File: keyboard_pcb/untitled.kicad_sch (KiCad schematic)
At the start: 39 parts, among them J1 USB_C_Receptacle_USB2.0_16P, J2 Conn_01x02, J3 SWD, SW1 Reset, U1 NCP1117-3.3_SOT223, U2 RP2040, U3 W25Q128JVS, Y1 Crystal_GND24

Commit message: completed all routing and ground fill
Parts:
- H1, H2, H3, H4: footprint Components:L60 Outline -> MountingHole:MountingHole_2.2mm_M2_DIN965_Pad
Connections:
- net RESET is gone; now on net Run: J3.1 (Pin_1)
- net SWDIO is gone; now on net SWD: J3.4 (Pin_4)
- net Run: now also U2.26 (RUN)
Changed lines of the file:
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@@
 	(wire
 		(pts
+			(xy 133.35 95.25) (xy 146.05 95.25)
+		)
+		(stroke
+			(width 0)
+			(type default)
+		)
+	)
+	(wire
+		(pts
 			(xy 41.91 22.86) (xy 64.77 22.86)
 		)
@@
 	(wire
 		(pts
+			(xy 133.35 92.71) (xy 146.05 92.71)
+		)
+		(stroke
+			(width 0)
+			(type default)
+		)
+	)
+	(wire
+		(pts
 			(xy 252.73 53.34) (xy 262.89 53.34)
 		)
@@
 	(wire
 		(pts
+			(xy 139.7 85.09) (xy 146.05 85.09)
+		)
+		(stroke
+			(width 0)
+			(type default)
+		)
+	)
+	(wire
+		(pts
 			(xy 97.79 44.45) (xy 97.79 46.99)
 		)
@@
 	(wire
 		(pts
+			(xy 195.58 53.34) (xy 201.93 53.34)
+		)
+		(stroke
+			(width 0)
+			(type default)
+		)
+	)
+	(wire
+		(pts
 			(xy 44.45 148.59) (xy 50.8 148.59)
 		)
@@
 	(wire
 		(pts
-			(xy 134.62 90.17) (xy 146.05 90.17)
+			(xy 125.73 90.17) (xy 146.05 90.17)
 		)
 		(stroke
@@
 		)
 	)
+	(label "Run"
+		(at 195.58 53.34 0)
+		(effects
+			(font
+				(size 1.27 1.27)
+			)
+			(justify left bottom)
+		)
+	)
 	(label "QSPI_SCLK"
 		(at 191.77 86.36 0)
@@
 		)
 	)
+	(label "Run"
+		(at 139.7 85.09 0)
+		(effects
+			(font
+				(size 1.27 1.27)
+			)
+			(justify left bottom)
+		)
+	)
 	(label "QSPI_SD1"
 		(at 191.77 78.74 0)
@@
 		)
 	)
+	(label "SWD"
+		(at 133.35 92.71 0)
+		(effects
+			(font
+				(size 1.27 1.27)
+			)
+			(justify left bottom)
+		)
+	)
 	(label "XOUT"
 		(at 64.77 40.64 180)
@@
 		)
 	)
+	(label "SWCLK"
+		(at 133.35 95.25 0)
+		(effects
+			(font
+				(size 1.27 1.27)
+			)
+			(justify left bottom)
+		)
+	)
 	(label "XIN"
 		(at 64.77 22.86 180)
@@
 		)
 	)
-	(global_label "SWDIO"
-		(shape input)
-		(at 146.05 92.71 180)
-		(fields_autoplaced yes)
-		(effects
-			(font
-				(size 1.27 1.27)
-			)
-			(justify right)
-		)
-		(property "Intersheetrefs" "${INTERSHEET_REFS}"
-			(at 137.7707 92.6306 0)
-			(effects
-				(font
-					(size 1.27 1.27)
-				)
-				(justify right)
-				(hide yes)
-			)
-		)
-	)
 	(global_label "col1"
 		(shape input)
@@
 		)
 	)
-	(global_label "SWCLK"
-		(shape input)
-		(at 146.05 95.25 180)
-		(fields_autoplaced yes)
-		(effects
-			(font
-				(size 1.27 1.27)
-			)
-			(justify right)
-		)
-		(property "Intersheetrefs" "${INTERSHEET_REFS}"
-			(at 137.4079 95.1706 0)
-			(effects
-				(font
-					(size 1.27 1.27)
-				)
-				(justify right)
-				(hide yes)
-			)
-		)
-	)
-	(global_label "RESET"
-		(shape input)
-		(at 146.05 85.09 180)
-		(fields_autoplaced yes)
-		(effects
-			(font
-				(size 1.27 1.27)
-			)
-			(justify right)
-		)
-		(property "Intersheetrefs" "${INTERSHEET_REFS}"
-			(at 137.8917 85.0106 0)
-			(effects
-				(font
-					(size 1.27 1.27)
-				)
-				(justify right)
-				(hide yes)
-			)
-		)
-	)
 	(global_label "LED"
 		(shape input)
@@
 			)
 		)
-		(property "Footprint" "Components:L60 Outline"
+		(property "Footprint" "MountingHole:MountingHole_2.2mm_M2_DIN965_Pad"
 			(at 135.89 128.27 0)
 			(effects
@@
 			)
 		)
-		(property "Footprint" "Components:L60 Outline"
+		(property "Footprint" "MountingHole:MountingHole_2.2mm_M2_DIN965_Pad"
 			(at 116.84 128.27 0)
 			(effects
@@
 	(symbol
 		(lib_id "power:GND")
-		(at 134.62 90.17 0)
+		(at 125.73 90.17 0)
 		(unit 1)
 		(exclude_from_sim no)
@@
 		(dnp no)
 		(property "Reference" "#PWR040"
-			(at 134.62 96.52 0)
+			(at 125.73 96.52 0)
 			(effects
 				(font
@@
 		)
 		(property "Value" "GND"
-			(at 134.62 93.98 0)
+			(at 125.73 93.98 0)
 			(effects
 				(font
@@
 		)
 		(property "Footprint" ""
-			(at 134.62 90.17 0)
+			(at 125.73 90.17 0)
 			(effects
 				(font
@@
 		)
 		(property "Datasheet" ""
-			(at 134.62 90.17 0)
+			(at 125.73 90.17 0)
 			(effects
 				(font
@@
 		)
 		(property "Description" ""
-			(at 134.62 90.17 0)
+			(at 125.73 90.17 0)
 			(effects
 				(font
@@
 			)
 		)
-		(property "Footprint" "Components:L60 Outline"
+		(property "Footprint" "MountingHole:MountingHole_2.2mm_M2_DIN965_Pad"
 			(at 135.89 116.84 0)
 			(effects
@@
 			)
 		)
-		(property "Footprint" "Components:L60 Outline"
+		(property "Footprint" "MountingHole:MountingHole_2.2mm_M2_DIN965_Pad"
 			(at 116.84 116.84 0)
 			(effects

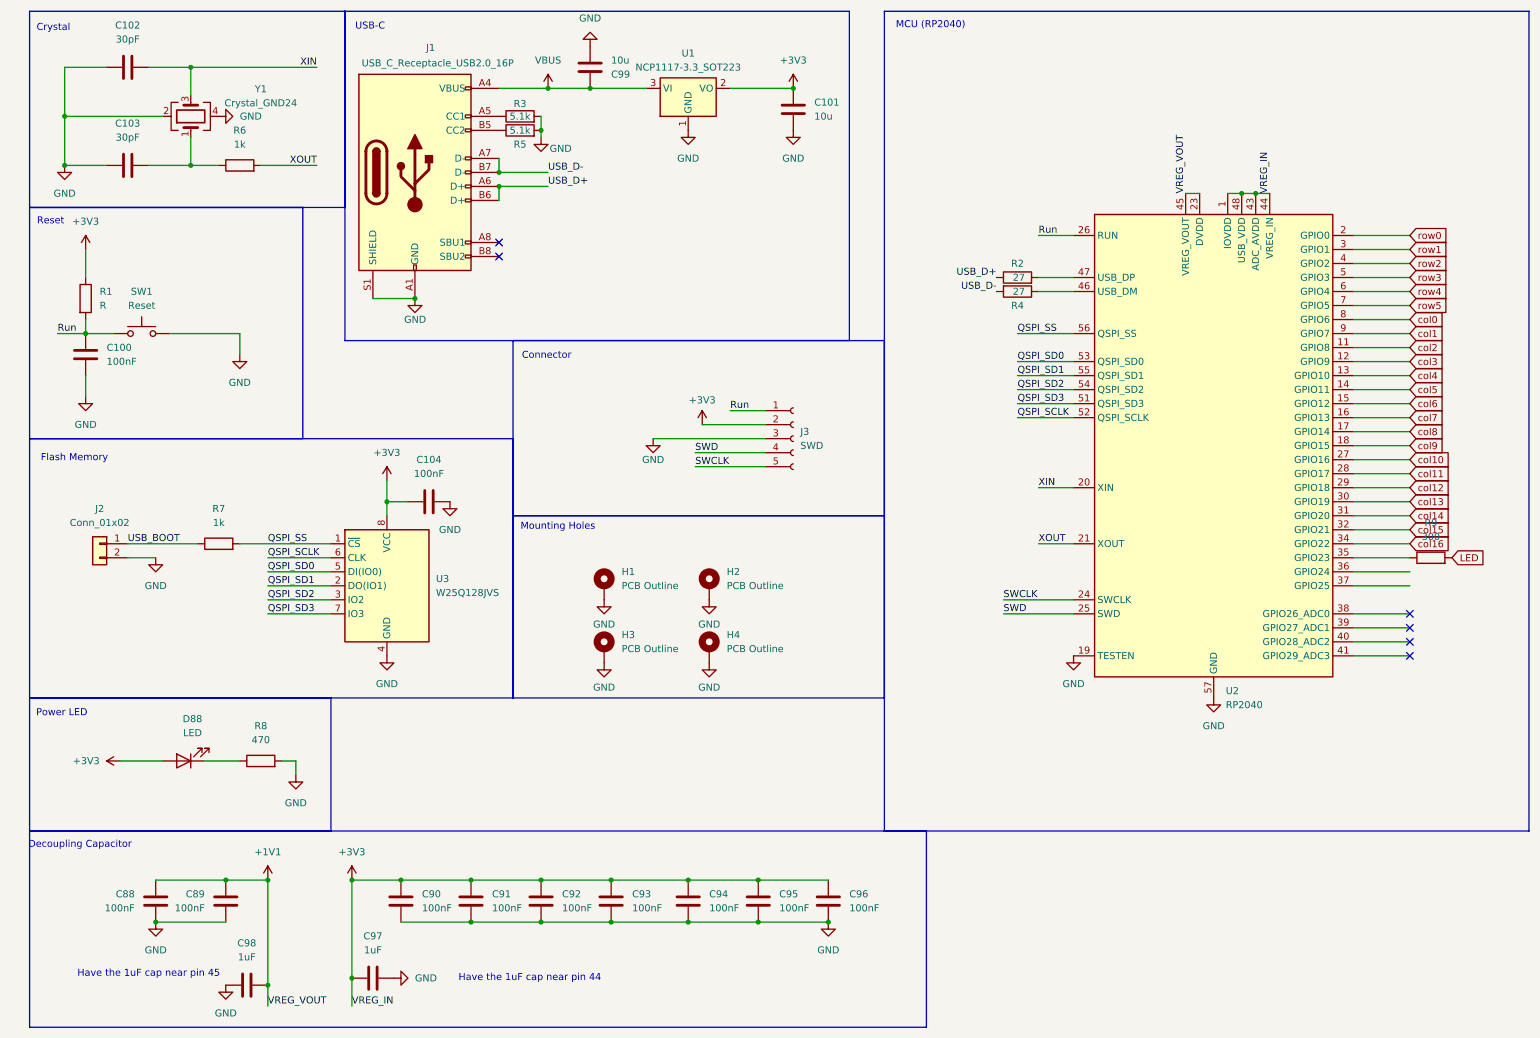
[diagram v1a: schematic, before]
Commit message: edited power supply circuits
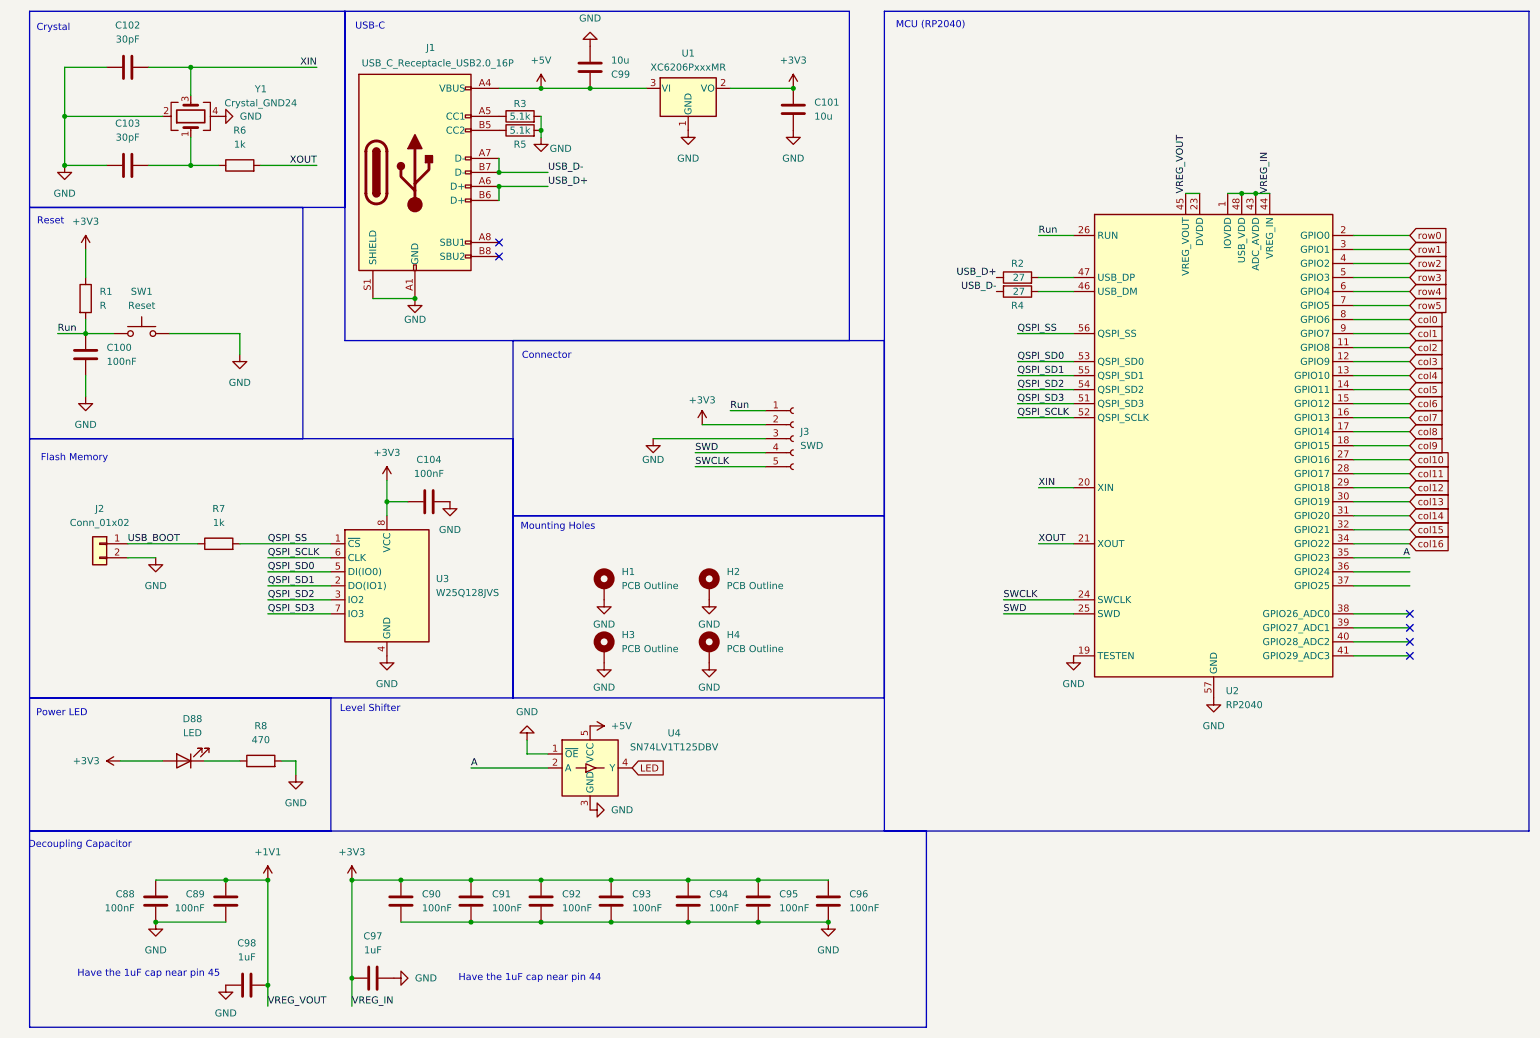
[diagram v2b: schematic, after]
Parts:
- removed R9: 300, Resistor_SMD:R_0603_1608Metric_Pad0.98x0.95mm_HandSolder, symbol Device:R
- removed U1: NCP1117-3.3_SOT223, Package_TO_SOT_SMD:SOT-223-3_TabPin2, symbol Regulator_Linear:NCP1117-3.3_SOT223
- added U1: XC6206PxxxMR, Package_TO_SOT_SMD:SOT-23-3, symbol Regulator_Linear:XC6206PxxxMR
- added U4: SN74LV1T125DBV, Package_TO_SOT_SMD:SOT-23-5, symbol Logic_LevelTranslator:SN74LV1T125DBV
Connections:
- net +3V3: now also U1.2 (VO)
- net GND: now also U1.1 (GND), U4.1 (~{OE}), U4.3 (GND)
- net LED: now also U4.4 (Y)
- net A: now reaches U2.35 (GPIO23)
- net A: now also U4.2 (A)
- net VBUS renamed +5V
- net +5V: now also U1.3 (VI), U4.5 (VCC)
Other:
- note added: "Level Shifter"

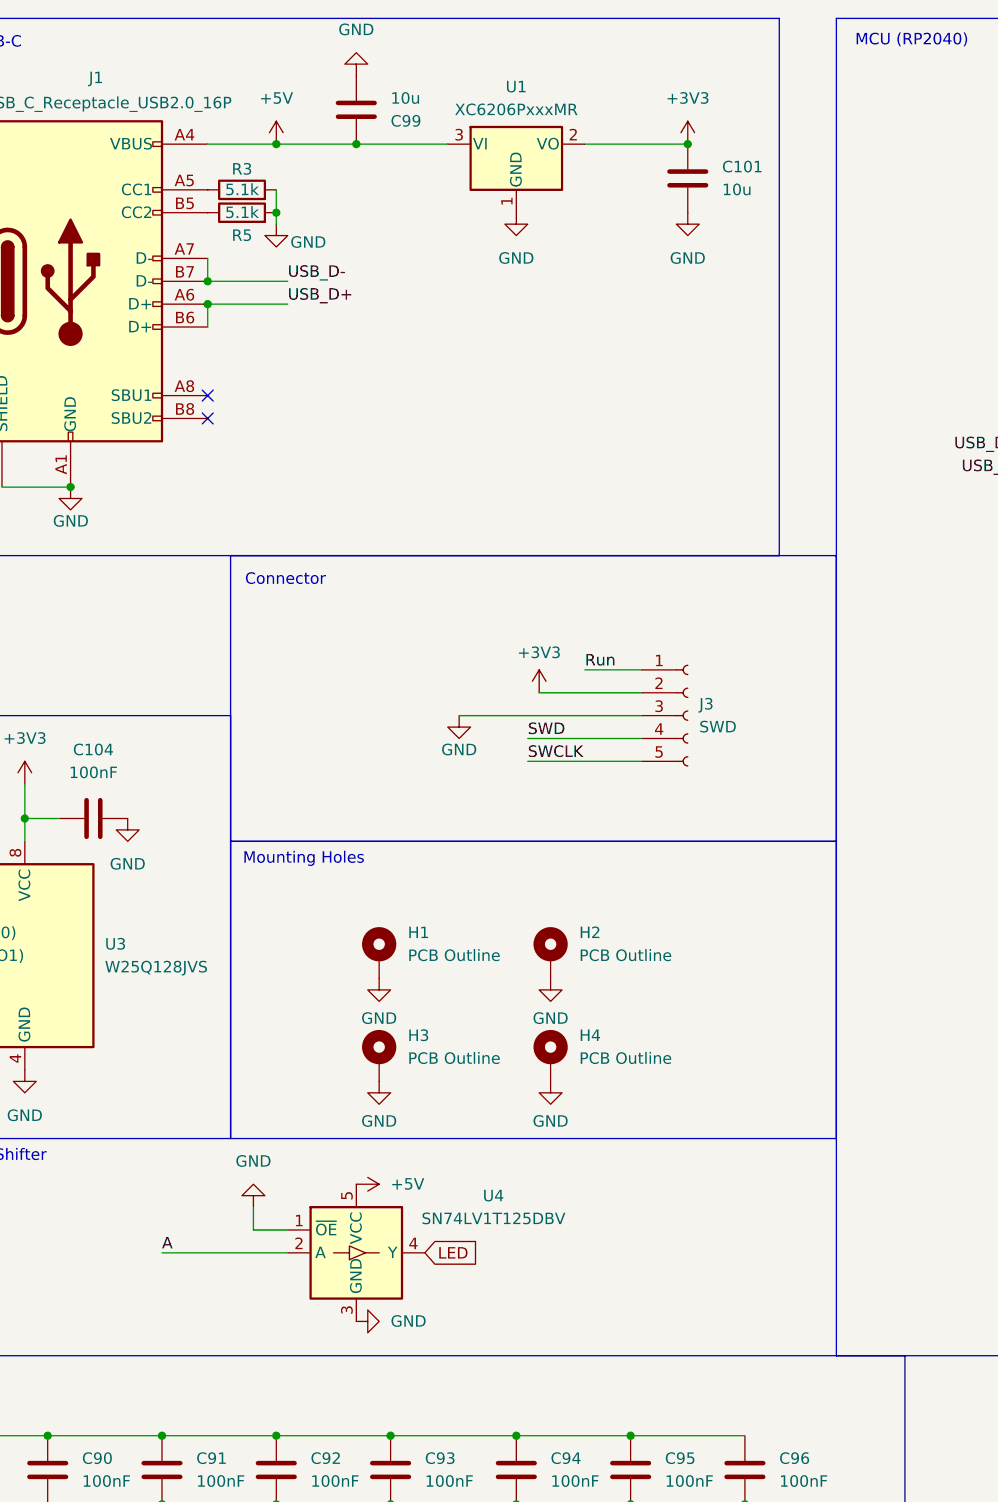
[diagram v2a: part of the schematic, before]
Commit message: reworked board outline
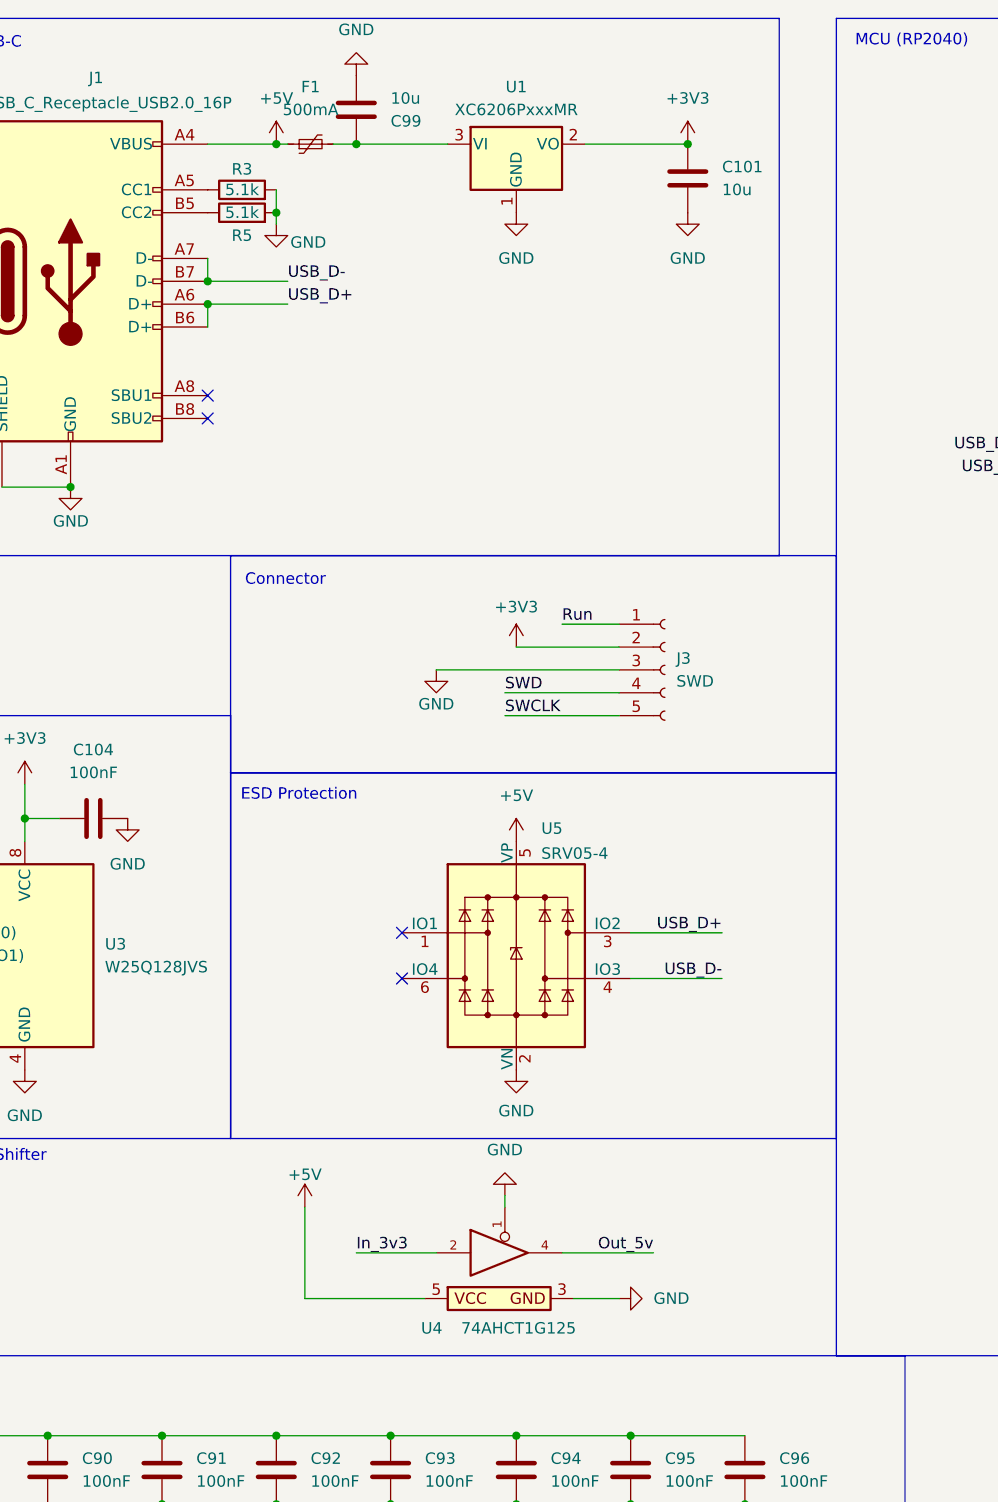
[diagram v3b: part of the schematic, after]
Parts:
- removed H1, H2, H3, H4: PCB Outline, MountingHole:MountingHole_2.2mm_M2_DIN965_Pad, symbol Mechanical:MountingHole_Pad
- removed U4: SN74LV1T125DBV, Package_TO_SOT_SMD:SOT-23-5, symbol Logic_LevelTranslator:SN74LV1T125DBV
- added F1: 500mA, Fuse:Fuse_1206_3216Metric, symbol Device:Polyfuse_Small
- added U4: 74AHCT1G125, Package_TO_SOT_SMD:SOT-23-5, symbol 74xGxx:74AHCT1G125
- added U5: SRV05-4, Package_TO_SOT_SMD:TSOT-23-6_HandSoldering, symbol marbastlib-various:SRV05-4
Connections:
- net +5V: now also F1.1, U4.5 (VCC), U5.5 (VP); no longer C99.1, U1.3 (VI)
- net GND: now also U4.1, U4.3 (GND), U5.2 (VN)
- net USB_D+: now also U5.3 (IO2)
- net USB_D-: now also U5.4 (IO3)
- new net: C99.1, F1.2, U1.3 (VI)
- new net In_3v3: U4.2
- new net Out_5v: U4.4
- new net VCC: U4.5 (VCC)
- no-connect marks 6 -> 8
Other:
- note added: "ESD Protection"
- note removed: "Mounting Holes"
- moved on the sheet: J3
